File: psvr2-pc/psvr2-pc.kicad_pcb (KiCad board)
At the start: 4 copper layers, 101.3 x 63.5 mm, 118 parts, among them IC1 SN65MLVD200D, IC2 SN65MLVD200D, J1 USB_C_Receptacle, J2 USB3_B_Micro, J3 DP_47272, J4 Barrel_Jack_Switch, J5 Conn_01x02_Pin, Q1 Si2301CDS, Q2 PN2222A, Q3 Si2301CDS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

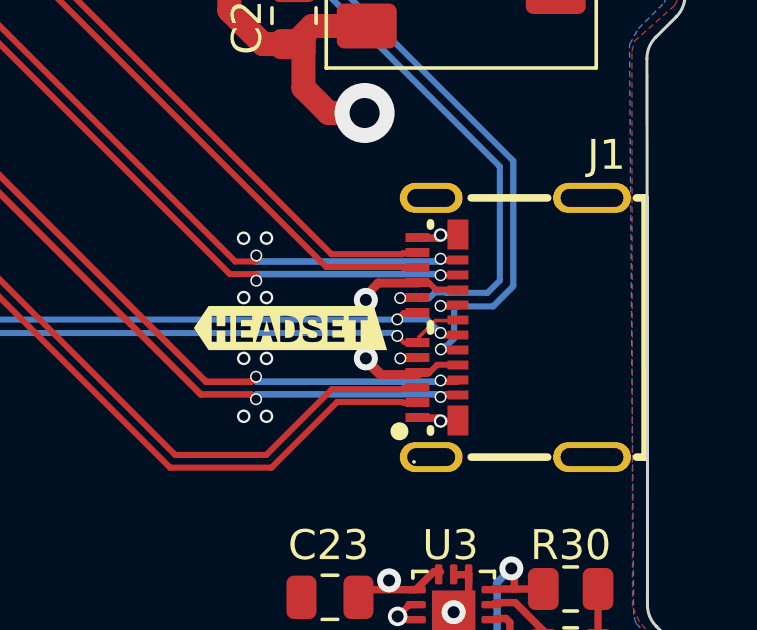
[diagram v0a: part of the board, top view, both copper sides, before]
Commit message: Fix the DRC error for the AUX pair now touching the safety area for a close via before starting with the skew tunning and squiggles.
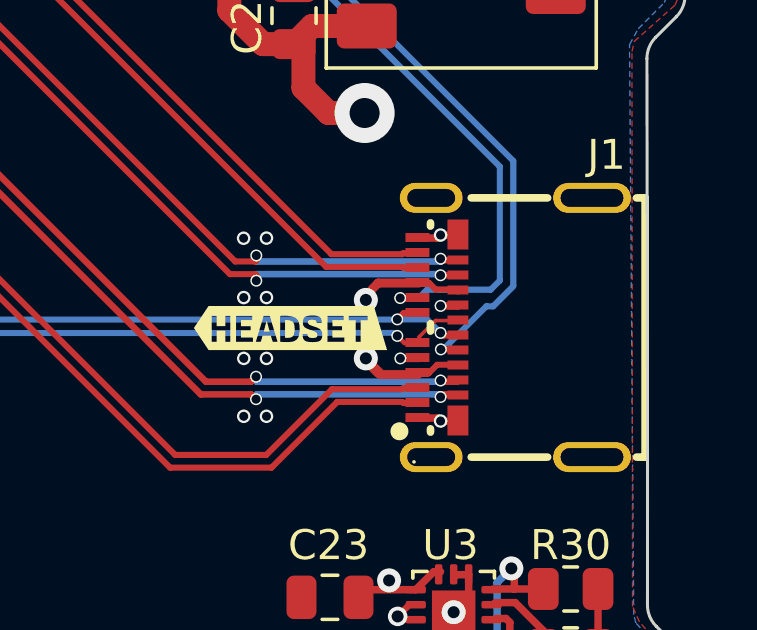
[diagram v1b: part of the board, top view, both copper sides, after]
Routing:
- net /HMD_AUX_N: track 41.1 -> 40.4 mm
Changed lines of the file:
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@@
   (segment (start 104.4956 42.688) (end 105.13 42.688) (width 0.2) (layer "F.Cu") (net 55))
   (via (at 104.4956 42.688) (size 0.4) (drill 0.3) (layers "F.Cu" "B.Cu") (net 55))
+  (segment (start 96.4118 26.9) (end 86.98 26.9) (width 0.2037) (layer "B.Cu") (net 55))
+  (segment (start 107.815 42.1068) (end 107.815 38.3032) (width 0.2037) (layer "B.Cu") (net 55))
   (segment (start 86.03 30.93) (end 86.38 30.93) (width 0.2037) (layer "B.Cu") (net 55))
-  (segment (start 105.466719 42.688) (end 105.654719 42.5) (width 0.2037) (layer "B.Cu") (net 55))
   (segment (start 85.06 27.96) (end 85.06 29.96) (width 0.2037) (layer "B.Cu") (net 55))
-  (segment (start 104.4956 42.688) (end 105.466719 42.688) (width 0.2037) (layer "B.Cu") (net 55))
-  (segment (start 107.4068 42.515) (end 107.815 42.1068) (width 0.2037) (layer "B.Cu") (net 55))
-  (segment (start 106.027513 42.5) (end 106.042513 42.515) (width 0.2037) (layer "B.Cu") (net 55))
   (segment (start 107.815 38.3032) (end 96.4118 26.9) (width 0.2037) (layer "B.Cu") (net 55))
-  (segment (start 105.654719 42.5) (end 106.027513 42.5) (width 0.2037) (layer "B.Cu") (net 55))
-  (segment (start 96.4118 26.9) (end 86.98 26.9) (width 0.2037) (layer "B.Cu") (net 55))
+  (segment (start 85.87 27.17) (end 85.13 27.91) (width 0.2037) (layer "B.Cu") (net 55))
+  (segment (start 86.71 27.17) (end 85.87 27.17) (width 0.2037) (layer "B.Cu") (net 55))
+  (segment (start 105.39 42.41) (end 107.5118 42.41) (width 0.2037) (layer "B.Cu") (net 55))
+  (segment (start 105.112 42.688) (end 105.39 42.41) (width 0.2037) (layer "B.Cu") (net 55))
   (segment (start 86.98 26.9) (end 86.71 27.17) (width 0.2037) (layer "B.Cu") (net 55))
-  (segment (start 86.71 27.17) (end 85.87 27.17) (width 0.2037) (layer "B.Cu") (net 55))
-  (segment (start 106.042513 42.515) (end 107.4068 42.515) (width 0.2037) (layer "B.Cu") (net 55))
-  (segment (start 85.87 27.17) (end 85.13 27.91) (width 0.2037) (layer "B.Cu") (net 55))
-  (segment (start 107.815 42.1068) (end 107.815 38.3032) (width 0.2037) (layer "B.Cu") (net 55))
+  (segment (start 107.5118 42.41) (end 107.815 42.1068) (width 0.2037) (layer "B.Cu") (net 55))
+  (segment (start 104.4956 42.688) (end 105.112 42.688) (width 0.2037) (layer "B.Cu") (net 55))
   (segment (start 85.06 29.96) (end 86.03 30.93) (width 0.2037) (layer "B.Cu") (net 55))
   (segment (start 106.391997 44.399997) (end 105.85 44.399997) (width 0.2) (layer "F.Cu") (net 56))
   (segment (start 106.43 44.438) (end 106.391997 44.399997) (width 0.2) (layer "F.Cu") (net 56))
   (via (at 105.85 44.399997) (size 0.4) (drill 0.3) (layers "F.Cu" "B.Cu") (net 56))
-  (segment (start 98.3282 28.18) (end 98.292943 28.18) (width 0.2037) (layer "B.Cu") (net 56))
-  (segment (start 85.02 23.5) (end 86.27 22.25) (width 0.2037) (layer "B.Cu") (net 56))
-  (segment (start 86.97 26.53) (end 86.6 26.16) (width 0.2037) (layer "B.Cu") (net 56))
-  (segment (start 106.027513 44.3) (end 106.291116 44.036397) (width 0.2037) (layer "B.Cu") (net 56))
-  (segment (start 86.975 26.525) (end 86.97 26.53) (width 0.2037) (layer "B.Cu") (net 56))
-  (segment (start 96.6732 26.525) (end 86.975 26.525) (width 0.2037) (layer "B.Cu") (net 56))
-  (segment (start 98.292943 28.18) (end 97.59 27.477057) (width 0.2037) (layer "B.Cu") (net 56))
-  (segment (start 106.291116 44.036397) (end 106.291116 42.965) (width 0.2037) (layer "B.Cu") (net 56))
-  (segment (start 85.77 26.16) (end 85.02 25.41) (width 0.2037) (layer "B.Cu") (net 56))
+  (segment (start 105.85 44.399997) (end 105.930132 44.399997) (width 0.2037) (layer "B.Cu") (net 56))
+  (segment (start 86.6 26.16) (end 85.77 26.16) (width 0.2037) (layer "B.Cu") (net 56))
   (segment (start 97.59 27.4418) (end 96.6732 26.525) (width 0.2037) (layer "B.Cu") (net 56))
   (segment (start 86.27 22.25) (end 86.38 22.25) (width 0.2037) (layer "B.Cu") (net 56))
+  (segment (start 85.02 23.5) (end 86.27 22.25) (width 0.2037) (layer "B.Cu") (net 56))
+  (segment (start 108.265 38.1168) (end 98.3282 28.18) (width 0.2037) (layer "B.Cu") (net 56))
+  (segment (start 105.930132 44.399997) (end 107.365129 42.965) (width 0.2037) (layer "B.Cu") (net 56))
+  (segment (start 85.02 25.41) (end 85.02 23.5) (width 0.2037) (layer "B.Cu") (net 56))
+  (segment (start 96.6732 26.525) (end 86.975 26.525) (width 0.2037) (layer "B.Cu") (net 56))
+  (segment (start 86.975 26.525) (end 86.97 26.53) (width 0.2037) (layer "B.Cu") (net 56))
+  (segment (start 107.365129 42.965) (end 107.5932 42.965) (width 0.2037) (layer "B.Cu") (net 56))
+  (segment (start 85.77 26.16) (end 85.02 25.41) (width 0.2037) (layer "B.Cu") (net 56))
   (segment (start 108.265 42.2932) (end 108.265 38.1168) (width 0.2037) (layer "B.Cu") (net 56))
-  (segment (start 85.02 25.41) (end 85.02 23.5) (width 0.2037) (layer "B.Cu") (net 56))
-  (segment (start 86.6 26.16) (end 85.77 26.16) (width 0.2037) (layer "B.Cu") (net 56))
+  (segment (start 97.59 27.477057) (end 97.59 27.4418) (width 0.2037) (layer "B.Cu") (net 56))
+  (segment (start 98.292943 28.18) (end 97.59 27.477057) (width 0.2037) (layer "B.Cu") (net 56))
+  (segment (start 86.97 26.53) (end 86.6 26.16) (width 0.2037) (layer "B.Cu") (net 56))
+  (segment (start 98.3282 28.18) (end 98.292943 28.18) (width 0.2037) (layer "B.Cu") (net 56))
   (segment (start 107.5932 42.965) (end 108.265 42.2932) (width 0.2037) (layer "B.Cu") (net 56))
-  (segment (start 105.85 44.399997) (end 105.85 44.3) (width 0.2037) (layer "B.Cu") (net 56))
-  (segment (start 105.85 44.3) (end 106.027513 44.3) (width 0.2037) (layer "B.Cu") (net 56))
-  (segment (start 108.265 38.1168) (end 98.3282 28.18) (width 0.2037) (layer "B.Cu") (net 56))
-  (segment (start 97.59 27.477057) (end 97.59 27.4418) (width 0.2037) (layer "B.Cu") (net 56))
-  (segment (start 106.291116 42.965) (end 107.5932 42.965) (width 0.2037) (layer "B.Cu") (net 56))
   (segment (start 37.76 17.04) (end 33.69 21.11) (width 0.2037) (layer "F.Cu") (net 58))
   (segment (start 29.750254 21.359746) (end 26.538509 21.359746) (width 0.2037) (layer "F.Cu") (net 58))

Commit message: I honestly don't remember what changed. :)
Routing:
- net /PC_INNER_AUX_P: track 28.8 -> 48.9 mm
- net /HMD_INNER_AUX_P: track 53.3 -> 68.7 mm
- net /HMD_AUX_P: track 39.5 -> 43.9 mm

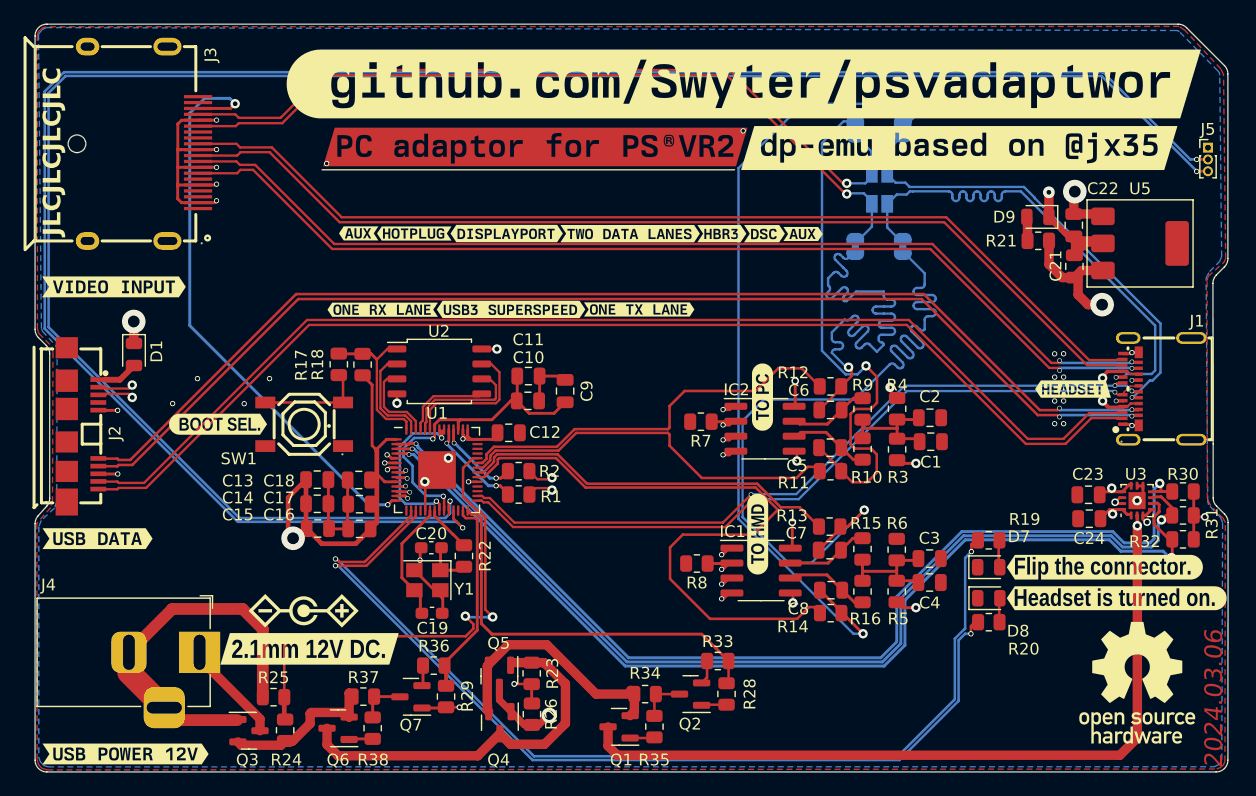
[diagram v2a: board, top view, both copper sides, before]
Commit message: Reorganized the tracks under the microcontroller to make them less messy. Now the vias aren't that close to the QFN thermal ground pad in the middle.
Now it looks more straightforward and all the related tracks go together.
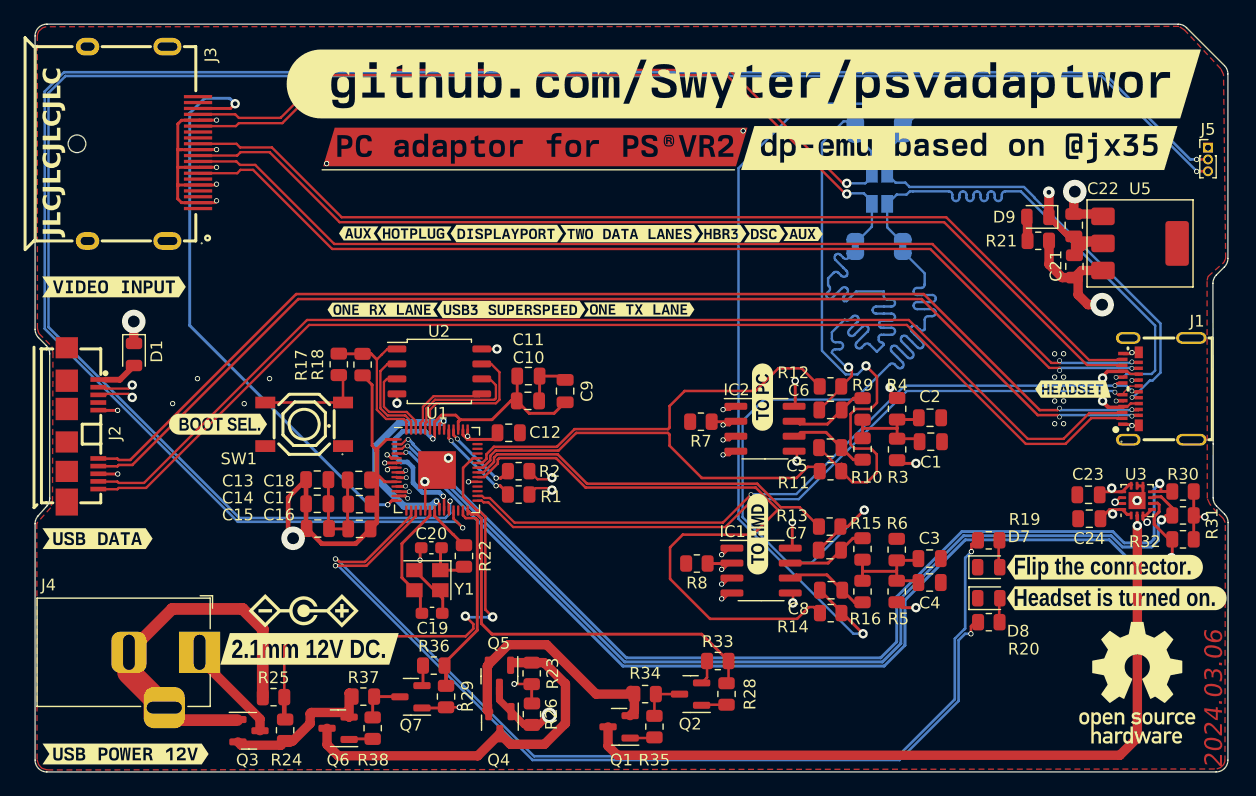
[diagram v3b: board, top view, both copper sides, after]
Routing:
- net +3.3V: track 91.8 -> 95.4 mm
- net +1V1: track 27.5 -> 30.2 mm
- net /PC_LVDS_R: track 39.3 -> 37.7 mm
- net /HMD_TYC_SDA: track 86.5 -> 87.2 mm
- removed copper zone on B.Cu, net GND

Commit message: Rename the project from psvadaptwor to psdaptwor for better SEO, we get PS Vita stuff with the PSV prefix.
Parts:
- removed kibuzzard-65C07BD2: G***, kibuzzard-65C07BD2
- added kibuzzard-65E91FE7: G***, kibuzzard-65E91FE7, F.Cu at (74.7, 17.6)

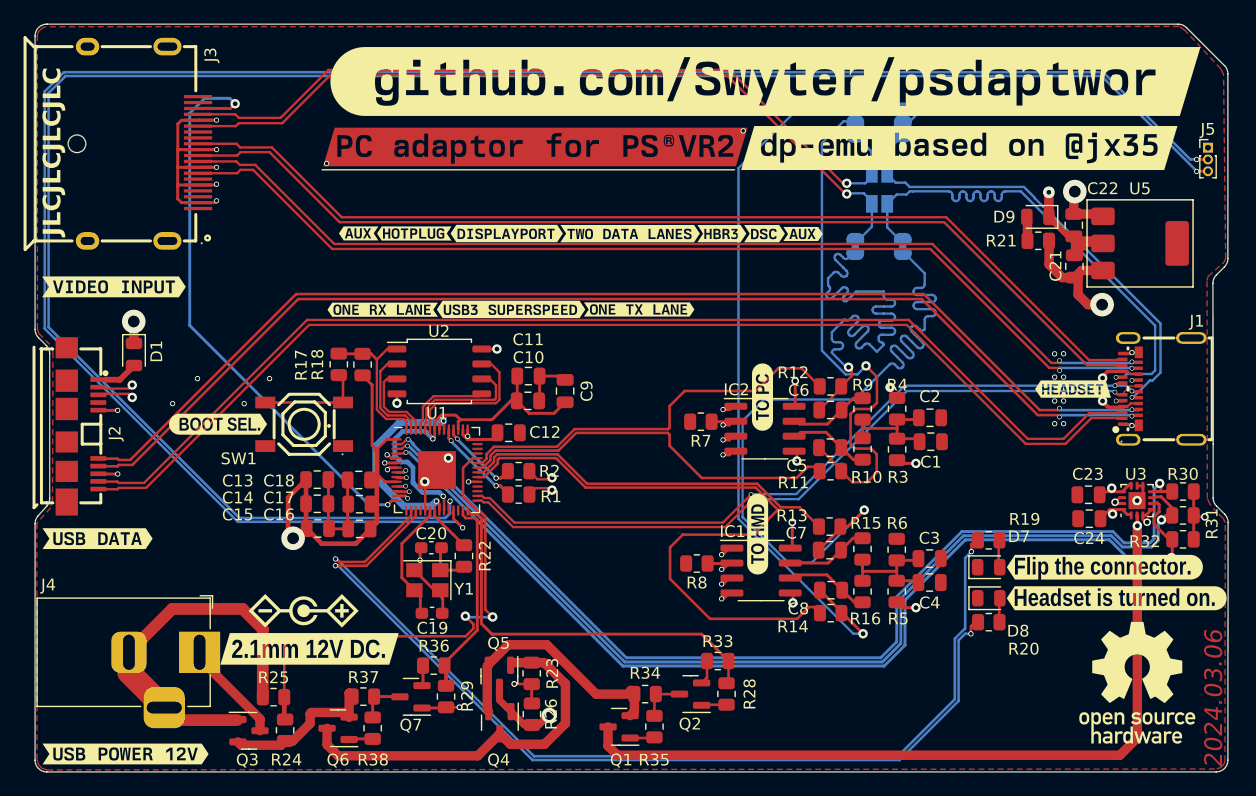
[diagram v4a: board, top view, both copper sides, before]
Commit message: Add three small 0.148mm tooling holes for SMT assembly and two big M4 ones, for any mounting shenanigans.
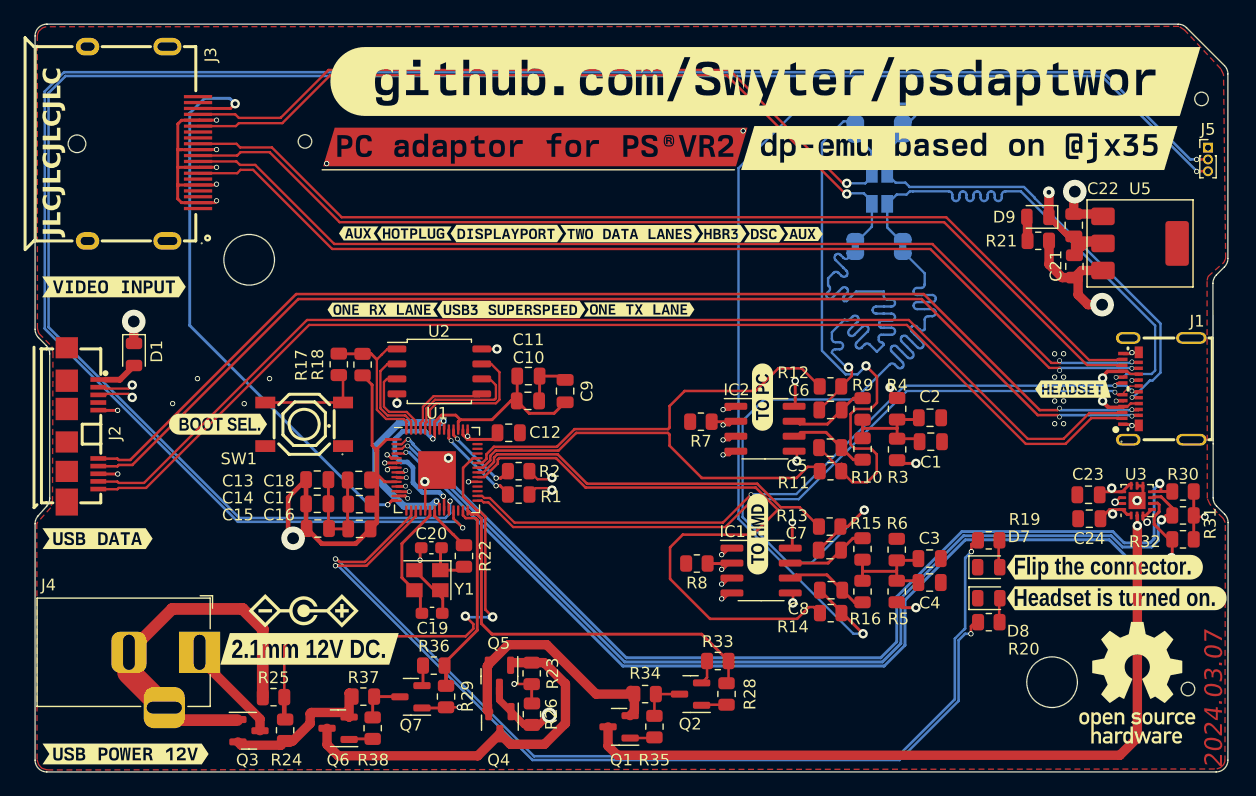
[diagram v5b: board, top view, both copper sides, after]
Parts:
- added ?: , , F.Cu at (110.6, 69.2)
- added ?: , , F.Cu at (111.8, 19.1)
- added ?: , , F.Cu at (30.9, 32.7)
- added REF**: MountingHole_2.1mm, MountingHole:MountingHole_2.1mm, F.Cu at (35.6, 22.7)
- added REF**: MountingHole_4.3mm_M4, MountingHole:MountingHole_4.3mm_M4, F.Cu at (99.1, 68.6)
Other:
- board text added: "2024.03.07"
- board text removed: "2024.03.06"
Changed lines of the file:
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@@
     )
   )
+  (footprint "" (layer "F.Cu")
+    (at 110.6 69.16)
+    (fp_text reference "" (at 0 0) (layer "F.SilkS")
+        (effects (font (size 1.27 1.27) (thickness 0.15)))
+    )
+    (fp_text value "" (at 0 0) (layer "F.SilkS")
+        (effects (font (size 1.27 1.27) (thickness 0.15)))
+    )
+    (pad "" np_thru_hole circle (at 0 0) (size 1.152 1.152) (drill 1.152) (layers "F&B.Cu" "*.Mask")
+      (solder_mask_margin 0.148) (clearance 0.148))
+  )
   (footprint "Resistor_SMD:R_0805_2012Metric" placed (layer "F.Cu")
     (at 110.1775 52.386)
@@
     (property "ki_keywords" "R resistor")
     (attr smd)
-    (fp_text reference "R31" (at 2.4715 0.7 90) (layer "F.SilkS")
+    (fp_text reference "R31" (at 2.3125 0.672 90) (layer "F.SilkS")
         (effects (font (size 1 1) (thickness 0.15)))
     )
@@
     )
   )
+  (footprint "" (layer "F.Cu")
+    (at 111.75 19.05)
+    (fp_text reference "" (at 0 0) (layer "F.SilkS")
+        (effects (font (size 1.27 1.27) (thickness 0.15)))
+    )
+    (fp_text value "" (at 0 0) (layer "F.SilkS")
+        (effects (font (size 1.27 1.27) (thickness 0.15)))
+    )
+    (pad "" np_thru_hole circle (at 0 0) (size 1.152 1.152) (drill 1.152) (layers "F&B.Cu" "*.Mask")
+      (solder_mask_margin 0.148) (clearance 0.148))
+  )
   (footprint "Capacitor_SMD:C_0805_2012Metric" placed (layer "F.Cu")
     (at 57.71 43.86 90)
@@
     )
   )
+  (footprint "MountingHole:MountingHole_2.1mm" (layer "F.Cu")
+    (at 35.62 22.66)
+    (descr "Mounting Hole 2.1mm, no annular")
+    (tags "mounting hole 2.1mm no annular")
+    (attr exclude_from_pos_files exclude_from_bom)
+    (fp_text reference "REF**" (at 0 -3.2) (layer "F.SilkS") hide
+        (effects (font (size 1 1) (thickness 0.15)))
+    )
+    (fp_text value "MountingHole_2.1mm" (at 0 3.2) (layer "F.Fab")
+        (effects (font (size 1 1) (thickness 0.15)))
+    )
+    (fp_text user "${REFERENCE}" (at 0 0) (layer "F.Fab")
+        (effects (font (size 1 1) (thickness 0.15)))
+    )
+    (fp_circle (center 0 0) (end 2.1 0)
+      (stroke (width 0.15) (type solid)) (fill none) (layer "Cmts.User"))
+    (fp_circle (center 0 0) (end 2.35 0)
+      (stroke (width 0.05) (type solid)) (fill none) (layer "F.CrtYd"))
+    (pad "" np_thru_hole circle (at 0 0) (size 1.152 1.152) (drill 1.152) (layers "F&B.Cu" "*.Mask")
+      (solder_mask_margin 0.148) (clearance 0.148))
+  )
   (footprint "Resistor_SMD:R_0805_2012Metric" placed (layer "F.Cu")
     (at 82.9675 48.775 -90)
@@
     )
   )
+  (footprint "MountingHole:MountingHole_4.3mm_M4" (layer "F.Cu")
+    (at 99.06 68.58)
+    (descr "Mounting Hole 4.3mm, no annular, M4")
+    (tags "mounting hole 4.3mm no annular m4")
+    (attr exclude_from_pos_files exclude_from_bom)
+    (fp_text reference "REF**" (at 0 -5.3) (layer "F.SilkS") hide
+        (effects (font (size 1 1) (thickness 0.15)))
+    )
+    (fp_text value "MountingHole_4.3mm_M4" (at 0 5.3) (layer "F.Fab")
+        (effects (font (size 1 1) (thickness 0.15)))
+    )
+    (fp_text user "${REFERENCE}" (at 0 0) (layer "F.Fab")
+        (effects (font (size 1 1) (thickness 0.15)))
+    )
+    (fp_circle (center 0 0) (end 4.3 0)
+      (stroke (width 0.15) (type solid)) (fill none) (layer "Cmts.User"))
+    (fp_circle (center 0 0) (end 4.55 0)
+      (stroke (width 0.05) (type solid)) (fill none) (layer "F.CrtYd"))
+    (pad "" np_thru_hole circle (at 0 0) (size 4.3 4.3) (drill 4.3) (layers "F&B.Cu" "*.Mask")
+      (solder_mask_margin 0.4) (clearance 0.5))
+  )
   (footprint "Resistor_SMD:R_0805_2012Metric" placed (layer "F.Cu")
     (at 32.95 69.85)
@@
     )
   )
+  (footprint "" (layer "F.Cu")
+    (at 30.88 32.71)
+    (fp_text reference "" (at 0 0) (layer "F.SilkS")
+        (effects (font (size 1.27 1.27) (thickness 0.15)))
+    )
+    (fp_text value "" (at 0 0) (layer "F.SilkS")
+        (effects (font (size 1.27 1.27) (thickness 0.15)))
+    )
+    (pad "" np_thru_hole circle (at 0 0) (size 4.3 4.3) (drill 4.3) (layers "F&B.Cu" "*.Mask")
+      (solder_mask_margin 0.4) (clearance 0.5))
+  )
   (footprint "kibuzzard-65E7A09E" (layer "F.Cu")
     (at 74.47 44.37 90)
@@
   (gr_line (start 112.72 34.704214) (end 112.74 48.33)
     (stroke (width 0.1) (type default)) (layer "Edge.Cuts"))
-  (gr_text "2024.03.06" (at 113.67 75.88 90) (layer "F.Cu")
+  (gr_text "2024.03.07" (at 113.67 75.88 90) (layer "F.Cu")
     (effects (font (size 1.5 1.5) (thickness 0.1875) italic) (justify left bottom))
   )
